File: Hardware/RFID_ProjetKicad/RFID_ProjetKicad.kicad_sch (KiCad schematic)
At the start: 1 part, among them U1 XIAO-ESP32-C6-DIP

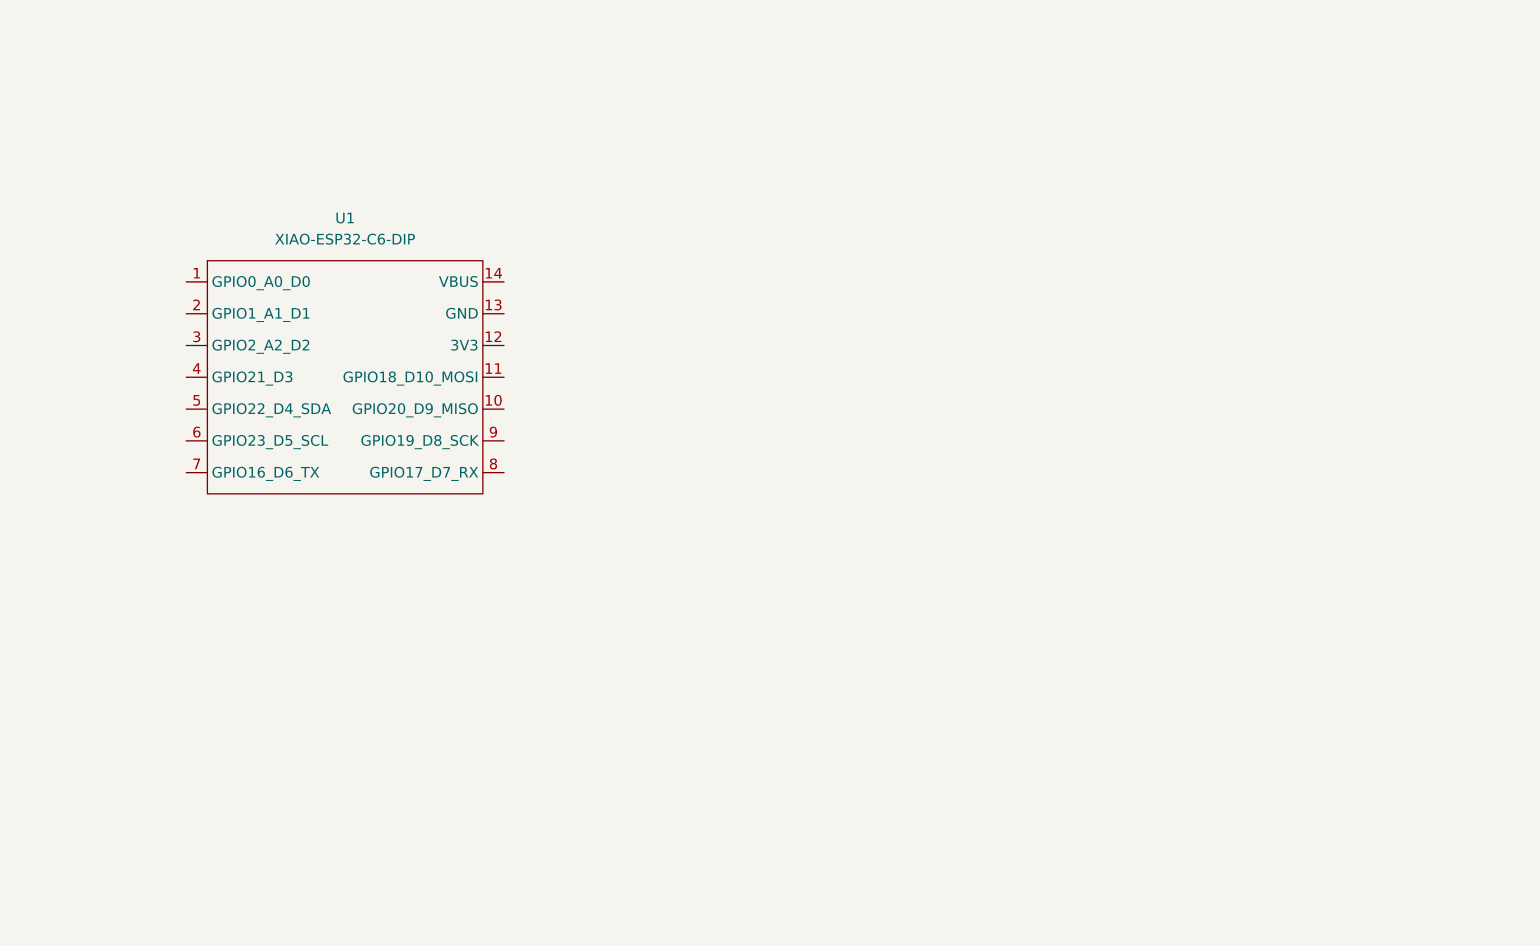
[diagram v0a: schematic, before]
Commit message: Création de la librairie du projet
Fusion des bibliotheques + suppression fichier inutiles
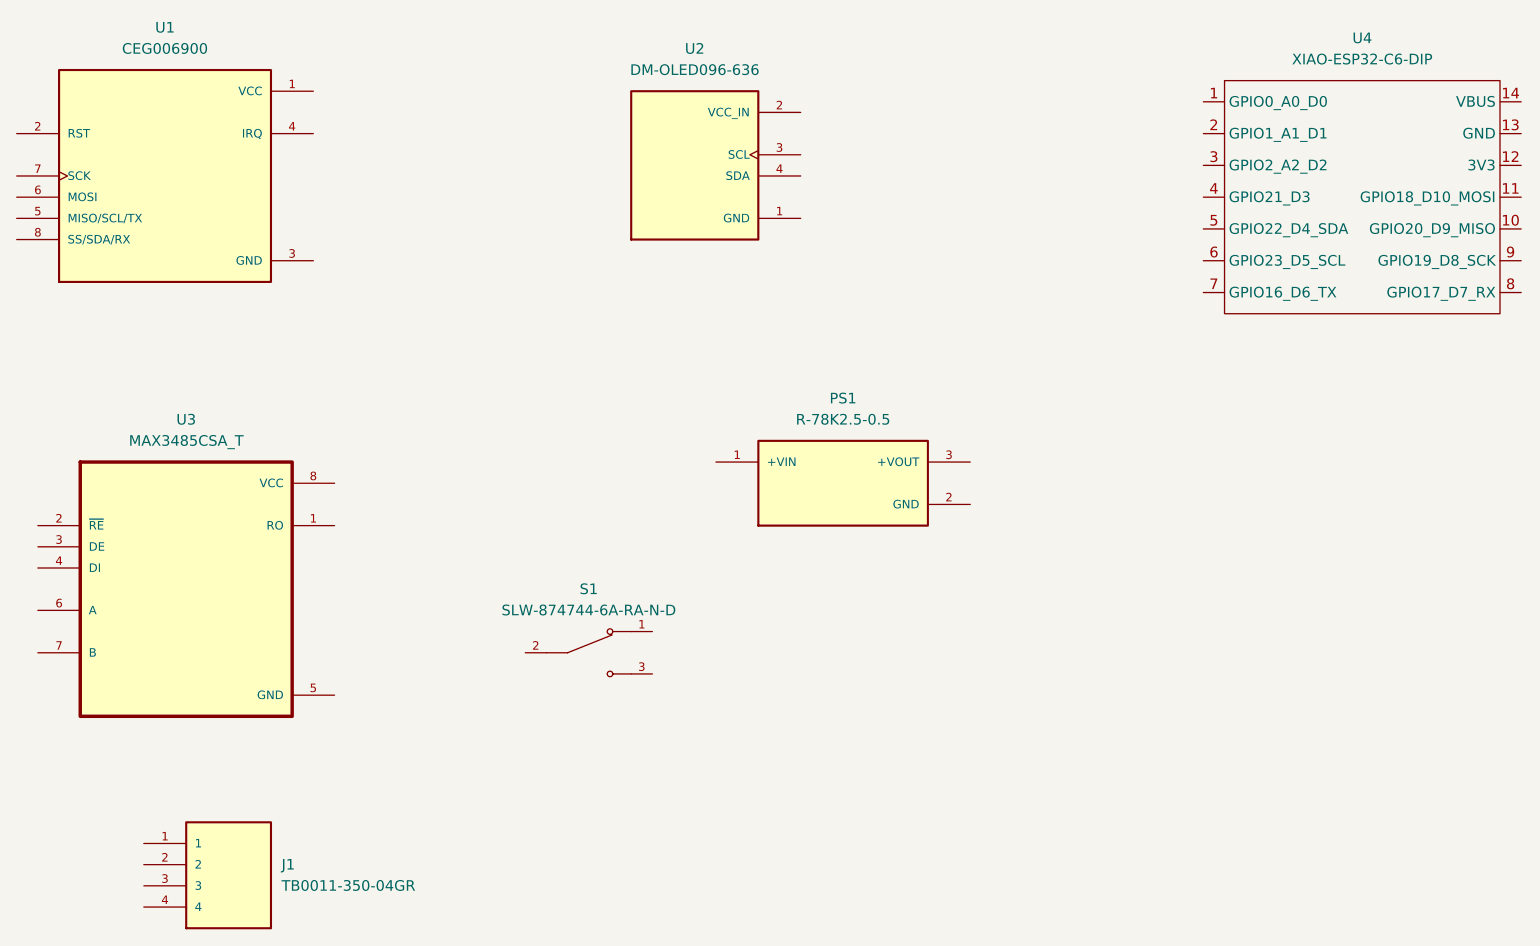
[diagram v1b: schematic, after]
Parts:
- removed U1: XIAO-ESP32-C6-DIP, Seeed Studio XIAO Series Library:XIAO-ESP32-C6-DIP, symbol Seeed_Studio_XIAO_Series:XIAO-ESP32-C6-DIP
- added J1: TB0011-350-04GR, RFID_Empreintes:SAMESKY_TB0011-350-04GR, symbol RFID_Symboles:TB0011-350-04GR
- added PS1: R-78K2.5-0.5, RFID_Empreintes:CONV_R-78K2.5-0.5, symbol RFID_Symboles:R-78K2.5-0.5
- added S1: SLW-874744-6A-RA-N-D, RFID_Empreintes:SW_SLW-874744-6A-RA-N-D, symbol RFID_Symboles:SLW-874744-6A-RA-N-D
- added U1: CEG006900, RFID_Empreintes:MODULE_CEG006900, symbol RFID_Symboles:CEG006900
- added U2: DM-OLED096-636, RFID_Empreintes:MODULE_DM-OLED096-636, symbol RFID_Symboles:DM-OLED096-636
- added U3: MAX3485CSA_T, RFID_Empreintes:SOIC127P600X175-8N, symbol RFID_Symboles:MAX3485CSA_T
- added U4: XIAO-ESP32-C6-DIP, RFID_Empreintes:XIAO-ESP32-C6-DIP, symbol RFID_Symboles:XIAO-ESP32-C6-DIP

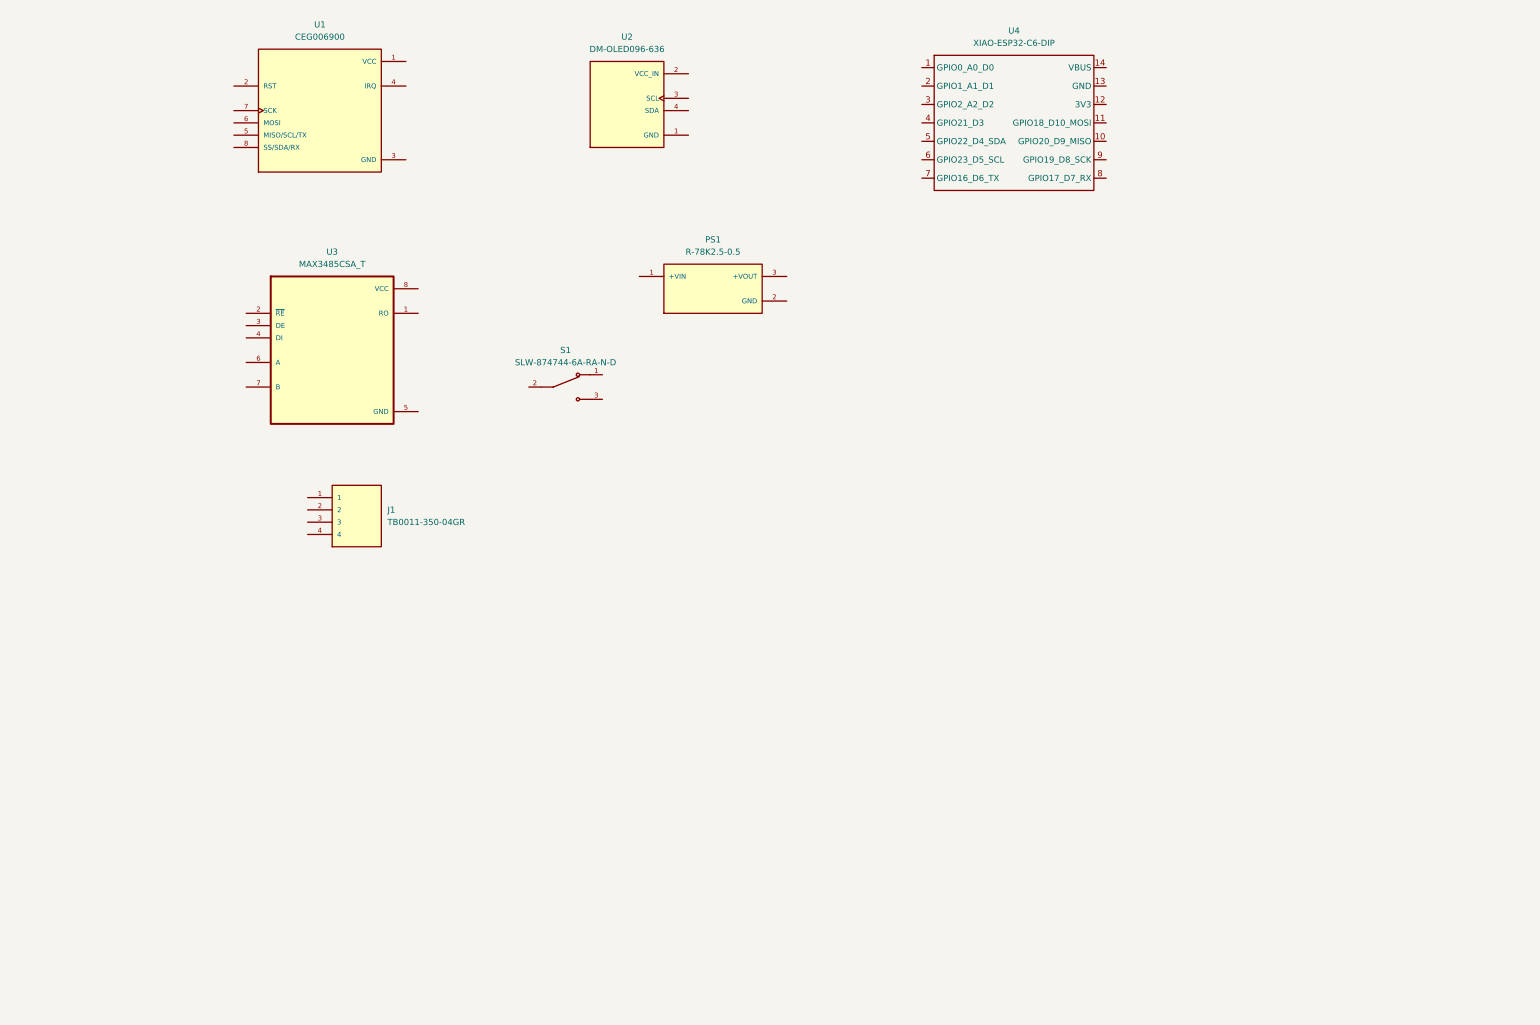
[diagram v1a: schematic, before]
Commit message: Ajout du schéma prototype d'ensemble
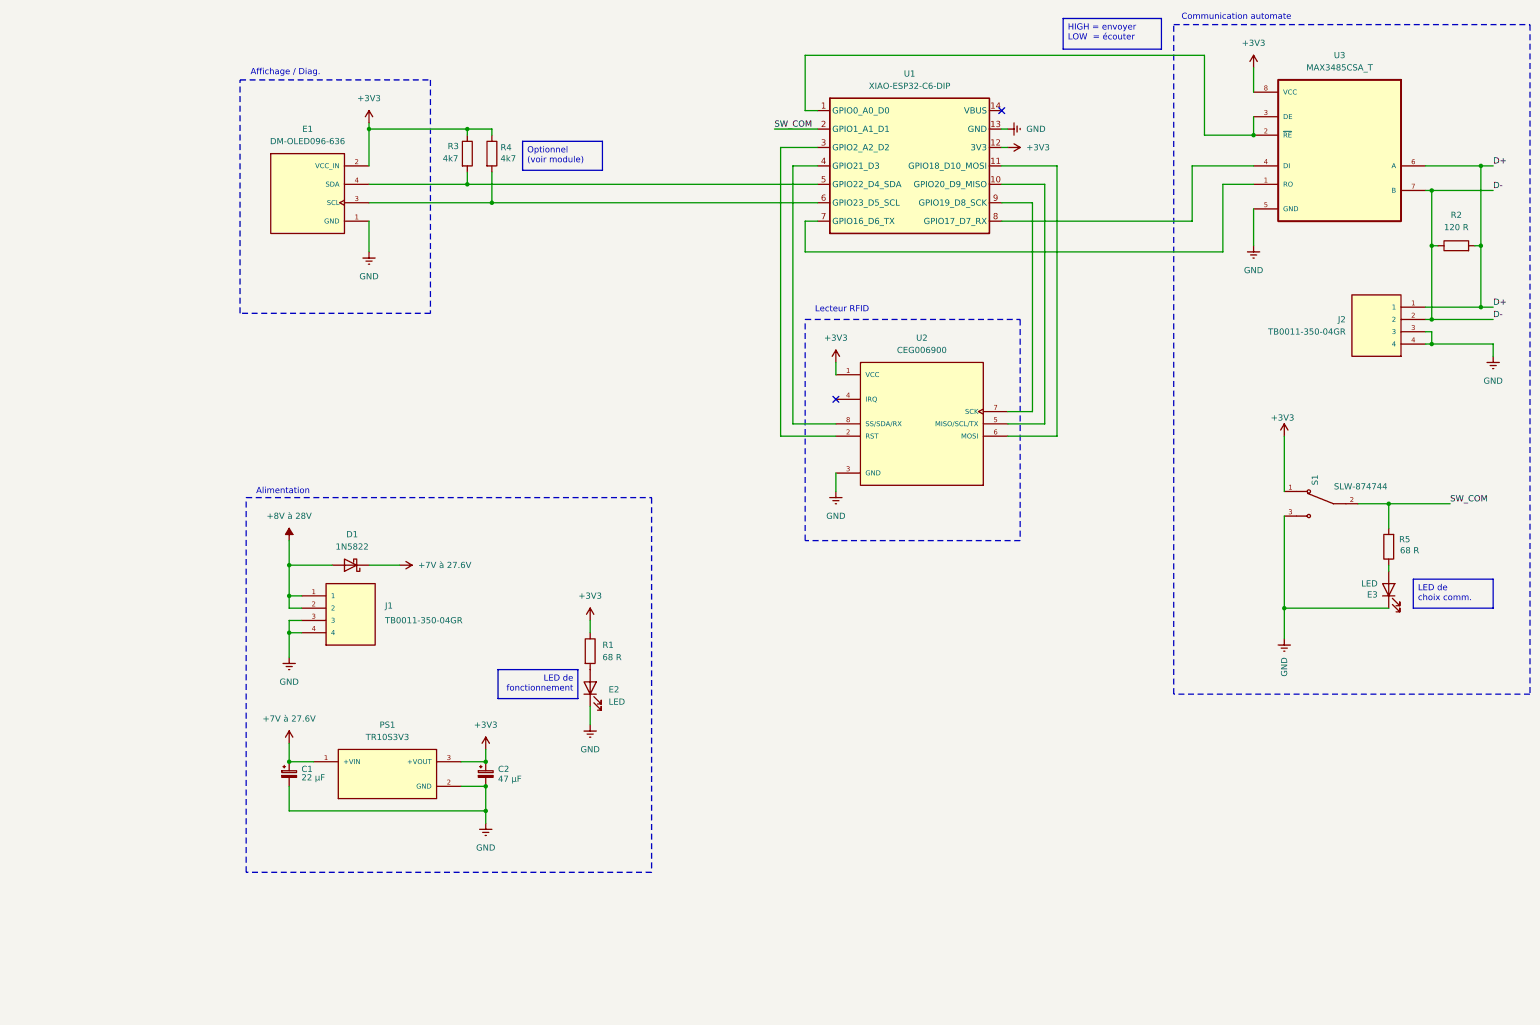
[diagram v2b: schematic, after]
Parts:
- removed U2: DM-OLED096-636, RFID_Empreintes:MODULE_DM-OLED096-636, symbol RFID_Symboles:DM-OLED096-636
- removed U4: XIAO-ESP32-C6-DIP, RFID_Empreintes:XIAO-ESP32-C6-DIP, symbol RFID_Symboles:XIAO-ESP32-C6-DIP
- added C1: 22 μF, symbol Device:C_Polarized_Small
- added C2: 47 μF, symbol Device:C_Polarized_Small
- added D1: 1N5822, Diode_THT:D_DO-201AD_P15.24mm_Horizontal, symbol Diode:1N5822
- added E1: DM-OLED096-636, symbol RFID_Symboles:DM-OLED096-636
- added E2, E3: LED, LED_SMD:LED_1206_3216Metric_Pad1.42x1.75mm_HandSolder, symbol Device:LED
- added J2: TB0011-350-04GR, RFID_Empreintes:SAMESKY_TB0011-350-04GR, symbol RFID_Symboles:TB0011-350-04GR
- added R1, R5: 68 R, Resistor_SMD:R_1206_3216Metric_Pad1.30x1.75mm_HandSolder, symbol Device:R
- added R2: 120 R, Resistor_SMD:R_1206_3216Metric_Pad1.30x1.75mm_HandSolder, symbol Device:R
- added R3, R4: 4k7, Resistor_SMD:R_1206_3216Metric_Pad1.30x1.75mm_HandSolder, symbol Device:R
- added U1: XIAO-ESP32-C6-DIP, RFID_Empreintes:XIAO-ESP32-C6-DIP, symbol RFID_Symboles:XIAO-ESP32-C6-DIP
- PS1: value R-78K2.5-0.5 -> TR10S3V3
- S1: value SLW-874744-6A-RA-N-D -> SLW-874744
- renumbered U1 to U2
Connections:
- net +3V3: now reaches U2.1 (VCC)
- net +3V3: now also PS1.3 (+VOUT), S1.1, U3.8 (VCC), C2.1, E1.2 (VCC_IN), R1.1, R3.1, R4.1, U1.12 (3V3)
- net at U2.2 (RST): now also U1.3 (GPIO2_A2_D2)
- net GND: now reaches U2.3 (GND)
- net GND: now also J1.3, J1.4, PS1.2 (GND), S1.3, U3.5 (GND), C1.2, C2.2, E1.1 (GND), E2.1 (K), E3.1 (K), J2.3, J2.4, U1.13 (GND)
- net at U2.5 (MISO/SCL/TX): now also U1.10 (GPIO20_D9_MISO)
- net at U2.6 (MOSI): now also U1.11 (GPIO18_D10_MOSI)
- net at U2.7 (SCK): now also U1.9 (GPIO19_D8_SCK)
- net at U2.8 (SS/SDA/RX): now also U1.4 (GPIO21_D3)
- net SW_COM: now reaches S1.2
- net SW_COM: now also R5.2, U1.2 (GPIO1_A1_D1)
- net at U3.1 (RO): now also U1.7 (GPIO16_D6_TX)
- net at U3.2 (~{RE}): now also U3.3 (DE), U1.1 (GPIO0_A0_D0)
- net at U3.4 (DI): now also U1.8 (GPIO17_D7_RX)
- net D+: now reaches U3.6 (A)
- net D+: now also J2.1, R2.2
- net D-: now reaches U3.7 (B)
- net D-: now also J2.2, R2.1
- net +7V à 27.6V: now reaches PS1.1 (+VIN)
- net +7V à 27.6V: now also C1.1, D1.1 (K)
- net +8V à 28V: now reaches J1.1
- net +8V à 28V: now also J1.2, D1.2 (A)
- new net: E1.4 (SDA), R3.2, U1.5 (GPIO22_D4_SDA)
- new net: E1.3 (SCL), R4.2, U1.6 (GPIO23_D5_SCL)
- new net: E2.2 (A), R1.2
- new net: E3.2 (A), R5.1
- no-connect marks 0 -> 2
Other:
- note added: "Affichage / Diag."
- note added: "Alimentation"
- note added: "Communication automate"
- note added: "Lecteur RFID"
- company: (none) -> École Supérieur Technique
- title: (none) -> M7 - Lecteur RFID
- moved on the sheet: J1, PS1, U2, U3

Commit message: Refactor de l'alimentation
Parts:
- removed C2: 47 μF, symbol Device:C_Polarized_Small
- added C2: 4.7μF, Capacitor_SMD:C_0201_0603Metric_Pad0.64x0.40mm_HandSolder, symbol Device:C_Small
- added C3: 10µF, Capacitor_SMD:C_0201_0603Metric_Pad0.64x0.40mm_HandSolder, symbol Device:C_Small
- added C4: 22µF, Capacitor_SMD:C_0201_0603Metric_Pad0.64x0.40mm_HandSolder, symbol Device:C_Small
- added D2: SMAJ28A, Diode_SMD:D_SMA, symbol Diode:SMAJ28A
- added F1: PTC 1A, symbol Device:Polyfuse
- added L1: 300 µH, symbol Device:L
- added L2: 5 mH, symbol Device:Filter_EMI_LL_1423
- added RV1: 20D470K, symbol Device:Varistor
- C1: value 22 μF -> 470µF
- D1: value 1N5822 -> BX36_R1
- PS1: value TR10S3V3 -> TSR 1-2433E
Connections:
- net +3V3: now also C4.1
- net +7V à 27.6V: now also D2.1 (A1), F1.2, L1.1, RV1.1; no longer C1.1, D1.1 (K), PS1.1 (+VIN)
- net GND: now also C2.2, C3.2, C4.2, D2.2 (A2), L2.1, L2.4, RV1.2
- new net: C1.1, C2.1, L1.2, L2.2
- new net: C3.1, L2.3, PS1.1 (+VIN)
- new net: D1.1 (K), F1.1
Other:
- note added: "3.3v 1A 3.3W"
- note added: "EMC : EN 55032 Classe B"
- note added: "P = 3.3w / 0.7 = 4.7w 7V I=P/U = 4.7 / 7 = 0.67 A"
- note added: "Vz = 28v"
- moved on the sheet: D1, E2, J1, PS1, R1

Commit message: Ajout de footprint + STEP files
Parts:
- removed PS1: TSR 1-2433E, RFID_Empreintes:CONV_R-78K2.5-0.5, symbol RFID_Symboles:R-78K2.5-0.5
- added PS1: TSR_1-2433E, RFID_Empreintes:CONV_TSR_1-2433E, symbol RFID_Symboles:TSR_1-2433E
- C1: footprint (none) -> Capacitor_THT:CP_Radial_D10.0mm_P5.00mm
- D1: footprint Diode_THT:D_DO-201AD_P15.24mm_Horizontal -> Diode_SMD:D_SMA_Handsoldering
- D2: footprint Diode_SMD:D_SMA -> Diode_SMD:D_SMA_Handsoldering
- L1: footprint (none) -> RFID_Empreintes:WE-FI_7447060
- L2: footprint (none) -> RFID_Empreintes:SS11VL-11050
- RV1: footprint (none) -> RFID_Empreintes:RV_Disc_D12mm_W4.7mm_P7.5mm
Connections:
- net +3V3: now also PS1.3 (+VOUT)
- net GND: now also PS1.2 (GND)
- net at C3.1, L2.3: now also PS1.1 (+VIN)
- net at U2.2 (RST): now also U1.1 (GPIO0_A0_D0); no longer U1.3 (GPIO2_A2_D2)
- net at U3.2 (~{RE}), U3.3 (DE): now also U1.3 (GPIO2_A2_D2); no longer U1.1 (GPIO0_A0_D0)
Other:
- note added: "Liaisons compatible avec XIAO ESP32-S3"

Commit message: Correction schéma et footprint
Test PCB 3D : OKEY!
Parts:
- E1: footprint (none) -> RFID_Empreintes:MODULE_DM-OLED096-636
- F1: footprint (none) -> RFID_Empreintes:PTC
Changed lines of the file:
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@@
 			)
 		)
-		(property "Footprint" ""
+		(property "Footprint" "RFID_Empreintes:MODULE_DM-OLED096-636"
 			(at 30.48 55.88 0)
 			(hide yes)
@@
 			)
 		)
-		(property "Footprint" ""
+		(property "Footprint" "RFID_Empreintes:PTC"
 			(at 62.23 111.76 0)
 			(hide yes)
